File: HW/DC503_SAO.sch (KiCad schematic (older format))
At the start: 21 parts, among them J1 GS2, J2 GS2, U1 ATTINY85-20SU, X1 Badgelife_shitty_connector

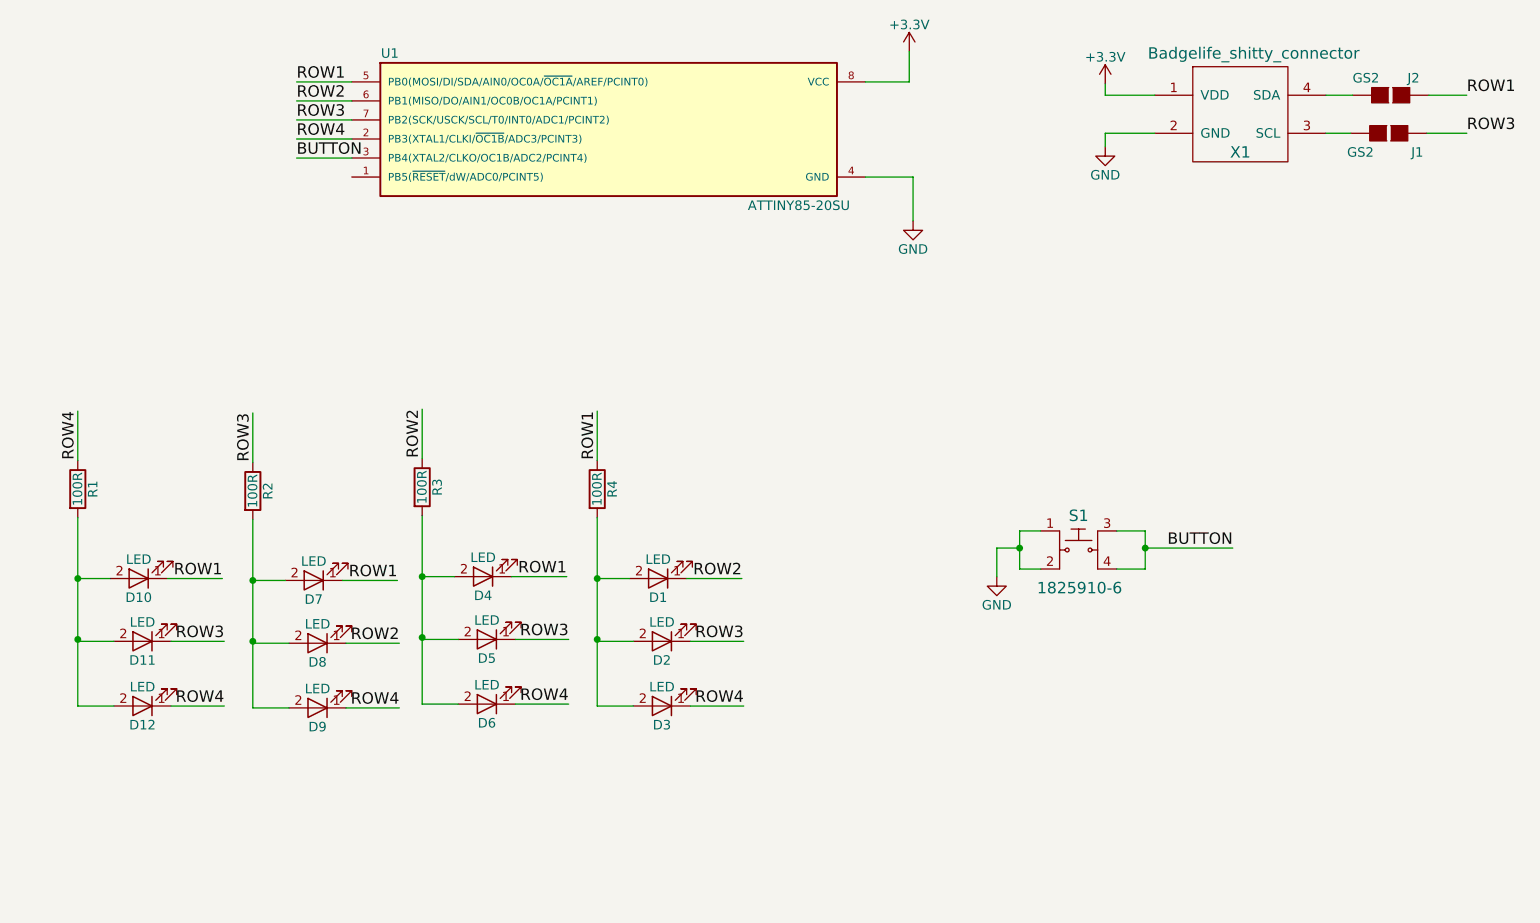
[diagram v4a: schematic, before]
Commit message: Fixed D12 wiring, Added Labels to LED nets
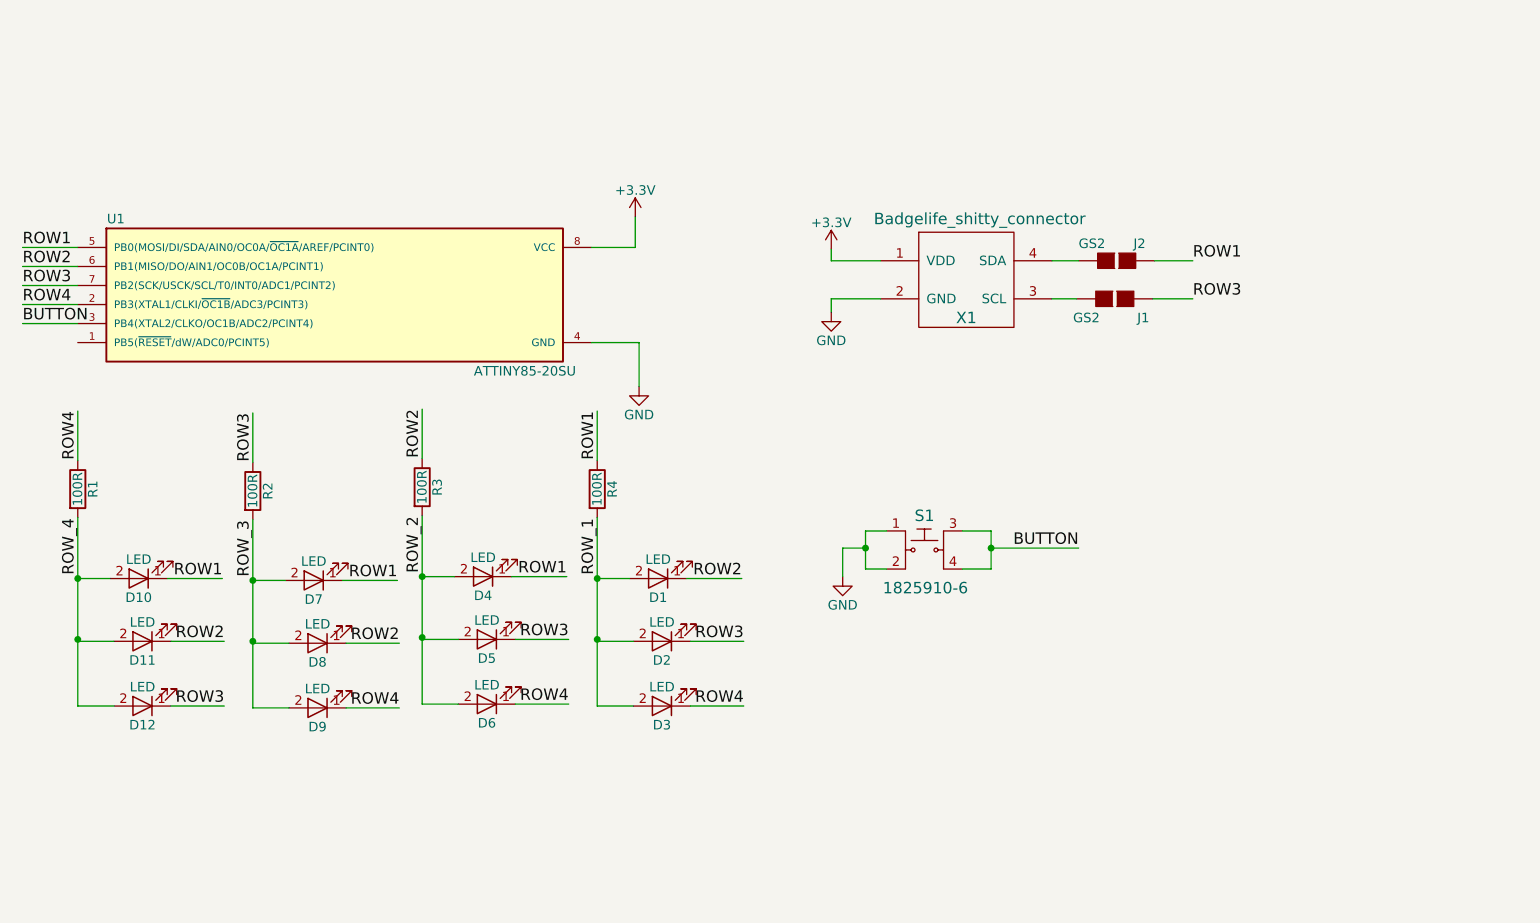
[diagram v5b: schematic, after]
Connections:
- net ROW2: now also D11.1 (K)
- net ROW3: now also D12.1 (K); no longer D11.1 (K)
- net ROW4: no longer D12.1 (K)
- net ROW_1: now reaches D1.2 (A), D2.2 (A), D3.2 (A), R4.2
- net ROW_2: now reaches D4.2 (A), D5.2 (A), D6.2 (A), R3.2
- net ROW_3: now reaches D7.2 (A), D8.2 (A), D9.2 (A), R2.2
- net ROW_4: now reaches D10.2 (A), D11.2 (A), D12.2 (A), R1.2
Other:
- moved on the sheet: J1, J2, S1, U1, X1
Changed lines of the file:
@@
 L ATTINY85-20SU U1
 U 1 1 5B4E7DA2
-P 6120 1770
-F 0 "U1" H 4970 2170 50  0000 C CNN
-F 1 "ATTINY85-20SU" H 7120 1370 50  0000 C CNN
-F 2 "Housings_SOIC:SOIC-8_3.9x4.9mm_Pitch1.27mm" H 7070 1770 50  0001 C CIN
-F 3 "" H 6120 1770 50  0001 C CNN
-	1    6120 1770
+P 4680 2640
+F 0 "U1" H 3530 3040 50  0000 C CNN
+F 1 "ATTINY85-20SU" H 5680 2240 50  0000 C CNN
+F 2 "Housings_SOIC:SOIC-8_3.9x4.9mm_Pitch1.27mm" H 5630 2640 50  0001 C CIN
+F 3 "" H 4680 2640 50  0001 C CNN
+	1    4680 2640
 	1    0    0    -1
 $EndComp
@@
 L Badgelife_shitty_connector X1
 U 1 1 5B4E7EF2
-P 9340 1690
-F 0 "X1" H 9440 1490 60  0000 C CNN
-F 1 "Badgelife_shitty_connector" H 9510 2010 60  0000 C CNN
-F 2 "SAO:Badgelife-Shitty-2x2" H 9340 1690 60  0001 C CNN
-F 3 "" H 9340 1690 60  0001 C CNN
-	1    9340 1690
+P 7900 2560
+F 0 "X1" H 8000 2360 60  0000 C CNN
+F 1 "Badgelife_shitty_connector" H 8070 2880 60  0000 C CNN
+F 2 "SAO:Badgelife-Shitty-2x2" H 7900 2560 60  0001 C CNN
+F 3 "" H 7900 2560 60  0001 C CNN
+	1    7900 2560
 	1    0    0    -1
 $EndComp
@@
 L GS2 J1
 U 1 1 5B4E8C34
-P 10220 1790
-F 0 "J1" V 10320 1940 50  0000 C CNN
-F 1 "GS2" V 10320 1641 50  0000 C CNN
-F 2 "Connectors:GS2" V 10294 1790 50  0001 C CNN
-F 3 "" H 10220 1790 50  0001 C CNN
-	1    10220 1790
+P 8780 2660
+F 0 "J1" V 8880 2810 50  0000 C CNN
+F 1 "GS2" V 8880 2511 50  0000 C CNN
+F 2 "Connectors:GS2" V 8854 2660 50  0001 C CNN
+F 3 "" H 8780 2660 50  0001 C CNN
+	1    8780 2660
 	0    1    1    0
 $EndComp
@@
 L GS2 J2
 U 1 1 5B4E8CEF
-P 10230 1590
-F 0 "J2" V 10140 1710 50  0000 C CNN
-F 1 "GS2" V 10140 1460 50  0000 C CNN
-F 2 "Connectors:GS2" V 10304 1590 50  0001 C CNN
-F 3 "" H 10230 1590 50  0001 C CNN
-	1    10230 1590
+P 8790 2460
+F 0 "J2" V 8700 2580 50  0000 C CNN
+F 1 "GS2" V 8700 2330 50  0000 C CNN
+F 2 "Connectors:GS2" V 8864 2460 50  0001 C CNN
+F 3 "" H 8790 2460 50  0001 C CNN
+	1    8790 2460
 	0    1    1    0
 $EndComp
@@
 L 1825910-6 S1
 U 1 1 5B4E90BD
-P 8590 3980
-F 0 "S1" H 8590 4160 60  0000 C CNN
-F 1 "1825910-6" H 8595 3780 60  0000 C CNN
-F 2 "digikey-footprints:Switch_Tactile_THT_6x6mm" H 8790 4180 60  0001 L CNN
-F 3 "http://www.te.com/commerce/DocumentDelivery/DDEController?Action=srchrtrv&DocNm=1825910&DocType=Customer+Drawing&DocLang=English" H 8790 4280 60  0001 L CNN
-F 4 "450-1650-ND" H 8790 4380 60  0001 L CNN "Digi-Key_PN"
-F 5 "1825910-6" H 8790 4480 60  0001 L CNN "MPN"
-F 6 "Switches" H 8790 4580 60  0001 L CNN "Category"
-F 7 "Tactile Switches" H 8790 4680 60  0001 L CNN "Family"
-F 8 "http://www.te.com/commerce/DocumentDelivery/DDEController?Action=srchrtrv&DocNm=1825910&DocType=Customer+Drawing&DocLang=English" H 8790 4780 60  0001 L CNN "DK_Datasheet_Link"
-F 9 "/product-detail/en/te-connectivity-alcoswitch-switches/1825910-6/450-1650-ND/1632536" H 8790 4880 60  0001 L CNN "DK_Detail_Page"
-F 10 "SWITCH TACTILE SPST-NO 0.05A 24V" H 8790 4980 60  0001 L CNN "Description"
-F 11 "TE Connectivity ALCOSWITCH Switches" H 8790 5080 60  0001 L CNN "Manufacturer"
-F 12 "Active" H 8790 5180 60  0001 L CNN "Status"
-	1    8590 3980
+P 7780 3980
+F 0 "S1" H 7780 4160 60  0000 C CNN
+F 1 "1825910-6" H 7785 3780 60  0000 C CNN
+F 2 "digikey-footprints:Switch_Tactile_THT_6x6mm" H 7980 4180 60  0001 L CNN
+F 3 "http://www.te.com/commerce/DocumentDelivery/DDEController?Action=srchrtrv&DocNm=1825910&DocType=Customer+Drawing&DocLang=English" H 7980 4280 60  0001 L CNN
+F 4 "450-1650-ND" H 7980 4380 60  0001 L CNN "Digi-Key_PN"
+F 5 "1825910-6" H 7980 4480 60  0001 L CNN "MPN"
+F 6 "Switches" H 7980 4580 60  0001 L CNN "Category"
+F 7 "Tactile Switches" H 7980 4680 60  0001 L CNN "Family"
+F 8 "http://www.te.com/commerce/DocumentDelivery/DDEController?Action=srchrtrv&DocNm=1825910&DocType=Customer+Drawing&DocLang=English" H 7980 4780 60  0001 L CNN "DK_Datasheet_Link"
+F 9 "/product-detail/en/te-connectivity-alcoswitch-switches/1825910-6/450-1650-ND/1632536" H 7980 4880 60  0001 L CNN "DK_Detail_Page"
+F 10 "SWITCH TACTILE SPST-NO 0.05A 24V" H 7980 4980 60  0001 L CNN "Description"
+F 11 "TE Connectivity ALCOSWITCH Switches" H 7980 5080 60  0001 L CNN "Manufacturer"
+F 12 "Active" H 7980 5180 60  0001 L CNN "Status"
+	1    7780 3980
 	1    0    0    -1
 $EndComp
@@
 L +3.3V #PWR01
 U 1 1 5B4EC8B1
-P 8730 1530
-F 0 "#PWR01" H 8730 1380 50  0001 C CNN
-F 1 "+3.3V" H 8730 1670 50  0000 C CNN
-F 2 "" H 8730 1530 50  0001 C CNN
-F 3 "" H 8730 1530 50  0001 C CNN
-	1    8730 1530
+P 7290 2400
+F 0 "#PWR01" H 7290 2250 50  0001 C CNN
+F 1 "+3.3V" H 7290 2540 50  0000 C CNN
+F 2 "" H 7290 2400 50  0001 C CNN
+F 3 "" H 7290 2400 50  0001 C CNN
+	1    7290 2400
 	1    0    0    -1
 $EndComp
@@
 L +3.3V #PWR02
 U 1 1 5B4EC905
-P 7700 1360
-F 0 "#PWR02" H 7700 1210 50  0001 C CNN
-F 1 "+3.3V" H 7700 1500 50  0000 C CNN
-F 2 "" H 7700 1360 50  0001 C CNN
-F 3 "" H 7700 1360 50  0001 C CNN
-	1    7700 1360
+P 6260 2230
+F 0 "#PWR02" H 6260 2080 50  0001 C CNN
+F 1 "+3.3V" H 6260 2370 50  0000 C CNN
+F 2 "" H 6260 2230 50  0001 C CNN
+F 3 "" H 6260 2230 50  0001 C CNN
+	1    6260 2230
 	1    0    0    -1
 $EndComp
@@
 L GND #PWR03
 U 1 1 5B4ECB98
-P 7720 2250
-F 0 "#PWR03" H 7720 2000 50  0001 C CNN
-F 1 "GND" H 7720 2100 50  0000 C CNN
-F 2 "" H 7720 2250 50  0001 C CNN
-F 3 "" H 7720 2250 50  0001 C CNN
-	1    7720 2250
+P 6280 3120
+F 0 "#PWR03" H 6280 2870 50  0001 C CNN
+F 1 "GND" H 6280 2970 50  0000 C CNN
+F 2 "" H 6280 3120 50  0001 C CNN
+F 3 "" H 6280 3120 50  0001 C CNN
+	1    6280 3120
 	1    0    0    -1
 $EndComp
@@
 L GND #PWR04
 U 1 1 5B4ECCFB
-P 8730 1860
-F 0 "#PWR04" H 8730 1610 50  0001 C CNN
-F 1 "GND" H 8730 1710 50  0000 C CNN
-F 2 "" H 8730 1860 50  0001 C CNN
-F 3 "" H 8730 1860 50  0001 C CNN
-	1    8730 1860
-	1    0    0    -1
-$EndComp
-Text Label 10630 1590 0    60   ~ 0
-ROW1
-Text Label 10630 1790 0    60   ~ 0
-ROW3
-Text Label 4480 1520 0    60   ~ 0
-ROW1
-Text Label 4480 1620 0    60   ~ 0
+P 7290 2730
+F 0 "#PWR04" H 7290 2480 50  0001 C CNN
+F 1 "GND" H 7290 2580 50  0000 C CNN
+F 2 "" H 7290 2730 50  0001 C CNN
+F 3 "" H 7290 2730 50  0001 C CNN
+	1    7290 2730
+	1    0    0    -1
+$EndComp
+Text Label 9190 2460 0    60   ~ 0
+ROW1
+Text Label 9190 2660 0    60   ~ 0
+ROW3
+Text Label 3040 2390 0    60   ~ 0
+ROW1
+Text Label 3040 2490 0    60   ~ 0
 ROW2
-Text Label 4480 1720 0    60   ~ 0
-ROW3
-Text Label 4480 1820 0    60   ~ 0
+Text Label 3040 2590 0    60   ~ 0
+ROW3
+Text Label 3040 2690 0    60   ~ 0
 ROW4
-Text Label 4480 1920 0    60   ~ 0
+Text Label 3040 2790 0    60   ~ 0
 BUTTON
-Text Label 9400 3970 2    60   ~ 0
+Text Label 8590 3970 2    60   ~ 0
 BUTTON
 Wire Wire Line
-	7470 1520 7700 1520
-Wire Wire Line
-	7700 1520 7700 1360
-Wire Wire Line
-	7470 2020 7720 2020
-Wire Wire Line
-	7720 2020 7720 2250
-Wire Wire Line
-	8730 1530 8730 1590
-Wire Wire Line
-	8730 1590 8990 1590
-Wire Wire Line
-	8730 1790 8730 1860
-Wire Wire Line
-	8730 1790 8990 1790
-Wire Wire Line
-	9890 1590 10030 1590
-Wire Wire Line
-	10020 1790 9890 1790
-Wire Wire Line
-	10430 1590 10630 1590
-Wire Wire Line
-	10420 1790 10630 1790
-Wire Wire Line
-	4770 1520 4480 1520
-Wire Wire Line
-	4770 1620 4480 1620
-Wire Wire Line
-	4770 1720 4480 1720
-Wire Wire Line
-	4770 1820 4480 1820
-Wire Wire Line
-	4480 1920 4770 1920
+	6030 2390 6260 2390
+Wire Wire Line
+	6260 2390 6260 2230
+Wire Wire Line
+	6030 2890 6280 2890
+Wire Wire Line
+	6280 2890 6280 3120
+Wire Wire Line
+	7290 2400 7290 2460
+Wire Wire Line
+	7290 2460 7550 2460
+Wire Wire Line
+	7290 2660 7290 2730
+Wire Wire Line
+	7290 2660 7550 2660
+Wire Wire Line
+	8450 2460 8590 2460
+Wire Wire Line
+	8580 2660 8450 2660
+Wire Wire Line
+	8990 2460 9190 2460
+Wire Wire Line
+	8980 2660 9190 2660
+Wire Wire Line
+	3330 2390 3040 2390
+Wire Wire Line
+	3330 2490 3040 2490
+Wire Wire Line
+	3330 2590 3040 2590
+Wire Wire Line
+	3330 2690 3040 2690
+Wire Wire Line
+	3040 2790 3330 2790
 Wire Wire Line
 	6230 4130 6060 4130
@@
 	6550 4800 6830 4800
 Wire Wire Line
-	8790 3880 8940 3880
-Wire Wire Line
-	8940 3880 8940 4080
-Wire Wire Line
-	8940 4080 8790 4080
-Wire Wire Line
-	8940 3970 9400 3970
-Connection ~ 8940 3970
-Wire Wire Line
-	8390 3880 8280 3880
-Wire Wire Line
-	8280 3880 8280 4080
-Wire Wire Line
-	8280 4080 8390 4080
-Wire Wire Line
-	8280 3970 8160 3970
-Wire Wire Line
-	8160 3970 8160 4120
-Connection ~ 8280 3970
+	7980 3880 8130 3880
+Wire Wire Line
+	8130 3880 8130 4080
+Wire Wire Line
+	8130 4080 7980 4080
+Wire Wire Line
+	8130 3970 8590 3970
+Connection ~ 8130 3970
+Wire Wire Line
+	7580 3880 7470 3880
+Wire Wire Line
+	7470 3880 7470 4080
+Wire Wire Line
+	7470 4080 7580 4080
+Wire Wire Line
+	7470 3970 7350 3970
+Wire Wire Line
+	7350 3970 7350 4120
+Connection ~ 7470 3970
 $Comp
 L GND #PWR05
 U 1 1 5B4F23B5
-P 8160 4120
-F 0 "#PWR05" H 8160 3870 50  0001 C CNN
-F 1 "GND" H 8160 3970 50  0000 C CNN
-F 2 "" H 8160 4120 50  0001 C CNN
-F 3 "" H 8160 4120 50  0001 C CNN
-	1    8160 4120
+P 7350 4120
+F 0 "#PWR05" H 7350 3870 50  0001 C CNN
+F 1 "GND" H 7350 3970 50  0000 C CNN
+F 2 "" H 7350 4120 50  0001 C CNN
+F 3 "" H 7350 4120 50  0001 C CNN
+	1    7350 4120
 	1    0    0    -1
 $EndComp
@@
 ROW1
 Text Label 4100 4460 2    60   ~ 0
-ROW3
+ROW2
 Text Label 4100 4800 2    60   ~ 0
-ROW4
+ROW3
+Text Label 3330 4110 1    60   ~ 0
+ROW_4
+Text Label 4250 4120 1    60   ~ 0
+ROW_3
+Text Label 5140 4100 1    60   ~ 0
+ROW_2
+Text Label 6060 4110 1    60   ~ 0
+ROW_1
 $EndSCHEMATC

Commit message: Updated Resistor refs to match their row number
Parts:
- renumbered R4 to R1, R3 to R2, R2 to R3, R1 to R4
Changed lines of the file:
@@
 $EndComp
 $Comp
-L R R4
+L R R1
 U 1 1 5B4E8222
 P 6060 3660
-F 0 "R4" V 6140 3660 50  0000 C CNN
+F 0 "R1" V 6140 3660 50  0000 C CNN
 F 1 "100R" V 6060 3660 50  0000 C CNN
 F 2 "Resistors_SMD:R_0805" V 5990 3660 50  0001 C CNN
@@
 ROW4
 $Comp
-L R R3
+L R R2
 U 1 1 5B4F2F35
 P 5140 3650
-F 0 "R3" V 5220 3650 50  0000 C CNN
+F 0 "R2" V 5220 3650 50  0000 C CNN
 F 1 "100R" V 5140 3650 50  0000 C CNN
 F 2 "Resistors_SMD:R_0805" V 5070 3650 50  0001 C CNN
@@
 ROW4
 $Comp
-L R R2
+L R R3
 U 1 1 5B4F3279
 P 4250 3670
-F 0 "R2" V 4330 3670 50  0000 C CNN
+F 0 "R3" V 4330 3670 50  0000 C CNN
 F 1 "100R" V 4250 3670 50  0000 C CNN
 F 2 "Resistors_SMD:R_0805" V 4180 3670 50  0001 C CNN
@@
 ROW4
 $Comp
-L R R1
+L R R4
 U 1 1 5B4F32A2
 P 3330 3660
-F 0 "R1" V 3410 3660 50  0000 C CNN
+F 0 "R4" V 3410 3660 50  0000 C CNN
 F 1 "100R" V 3330 3660 50  0000 C CNN
 F 2 "Resistors_SMD:R_0805" V 3260 3660 50  0001 C CNN

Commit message: Changed resistor and tiny85 foot prints. Roated SAO connector and fixed traces. Still missing ground vias.
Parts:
- X1: footprint SAO:Badgelife-Shitty-2x2 -> DC503_SAO:Badgelife-Shitty-2x2
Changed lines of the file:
@@
 F 0 "X1" H 8000 2360 60  0000 C CNN
 F 1 "Badgelife_shitty_connector" H 8070 2880 60  0000 C CNN
-F 2 "SAO:Badgelife-Shitty-2x2" H 7900 2560 60  0001 C CNN
+F 2 "DC503_SAO:Badgelife-Shitty-2x2" H 7900 2560 60  0001 C CNN
 F 3 "" H 7900 2560 60  0001 C CNN
 	1    7900 2560

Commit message: Updatedd files to KiCad 5.0. Added heart back to top.
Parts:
- D1, D10, D11, D12, D2, D3, D4, D5, D6, D7, D8, D9: symbol LED -> DC503_SAO-rescue:LED
- J1, J2: symbol GS2 -> DC503_SAO-rescue:GS2
- R1, R2, R3, R4: symbol R -> DC503_SAO-rescue:R
- S1: symbol 1825910-6 -> DC503_SAO-rescue:1825910-6
- U1: symbol ATTINY85-20SU -> DC503_SAO-rescue:ATTINY85-20SU
- X1: symbol Badgelife_shitty_connector -> DC503_SAO-rescue:Badgelife_shitty_connector
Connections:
- wire segments 62 -> 64
